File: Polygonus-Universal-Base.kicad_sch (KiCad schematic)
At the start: 11 parts, among them J1 Conn_02x04_Top_Bottom, J4 Polygonus_Plugs, J5 Conn_02x04_Top_Bottom, U1 WBO-Single-Module, U14 WBO-Single-Module

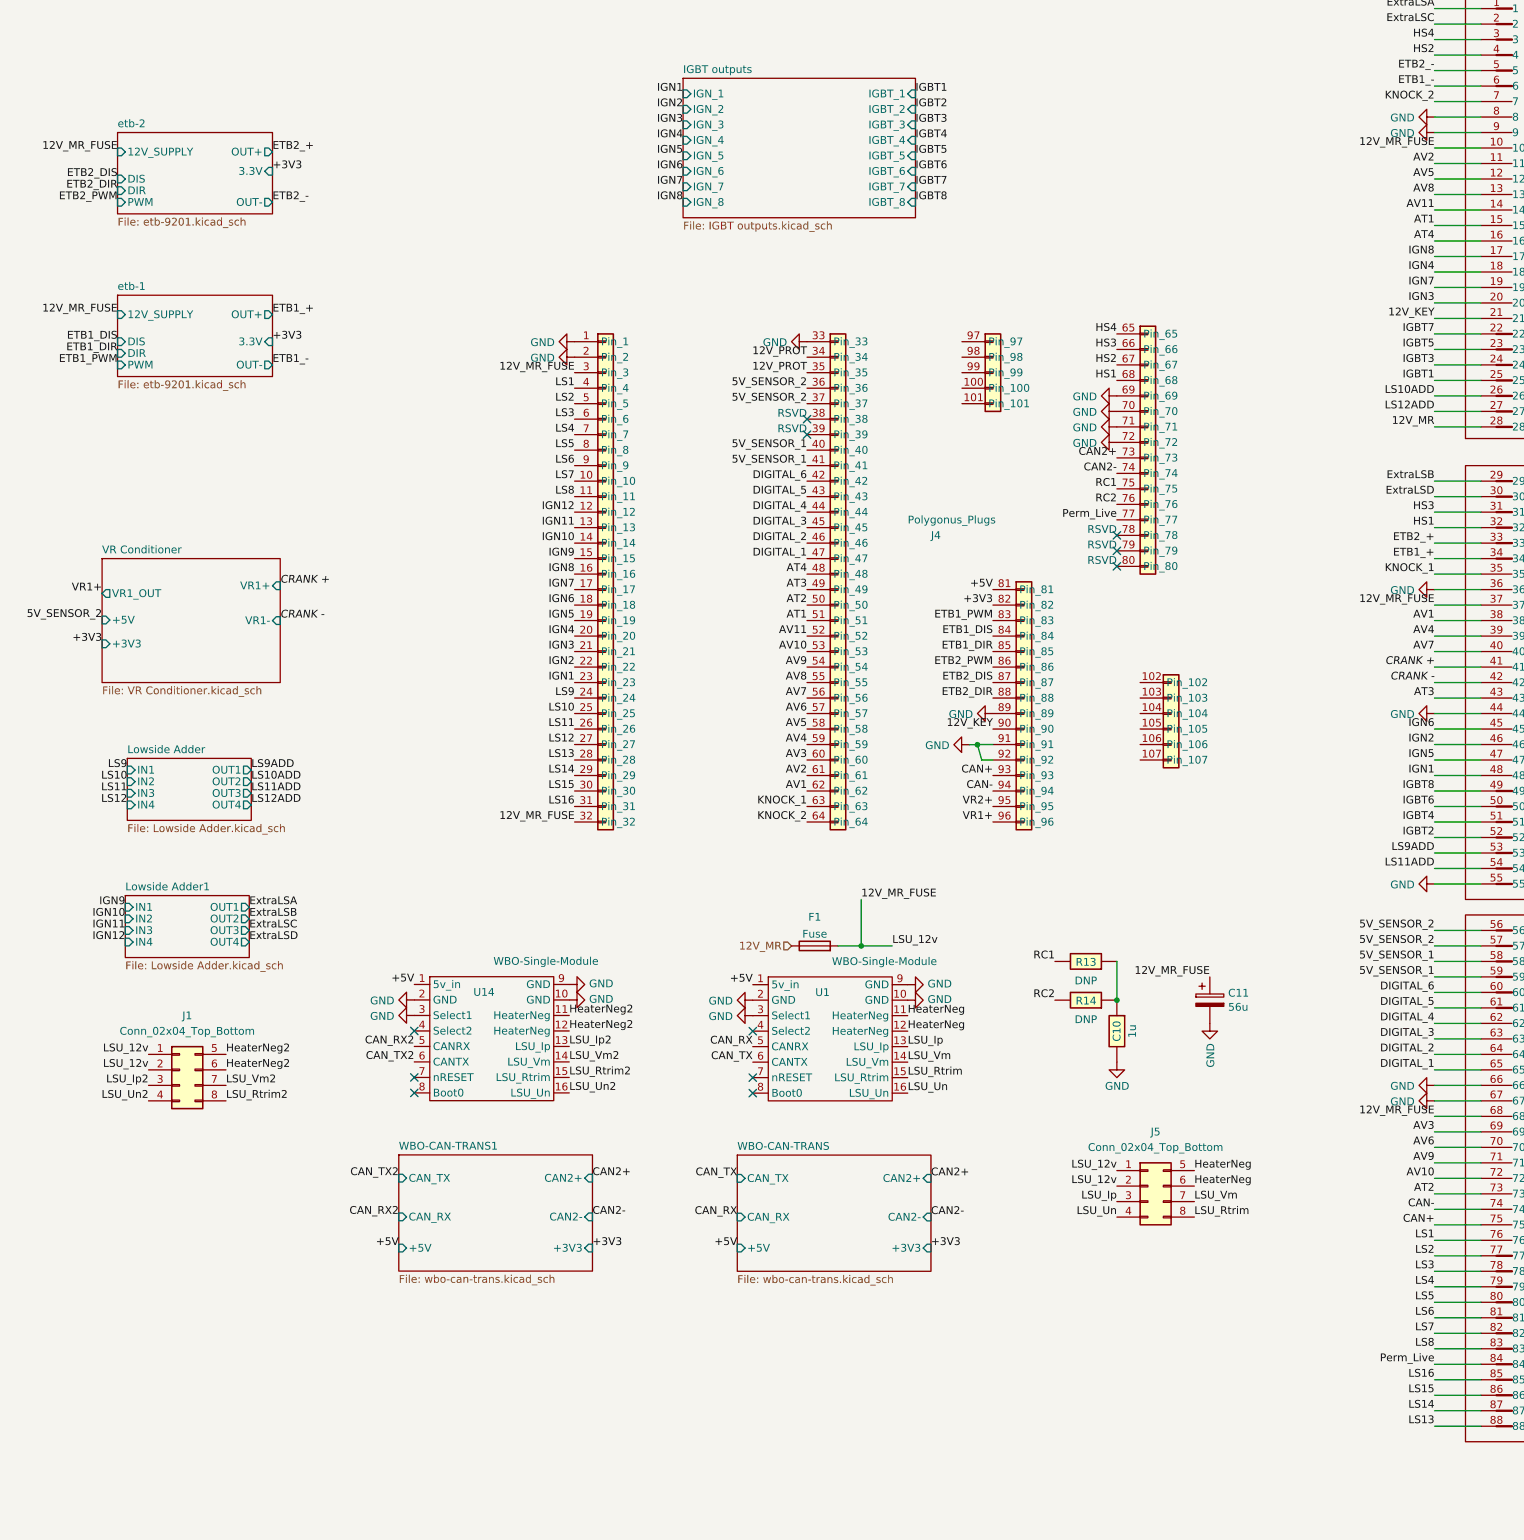
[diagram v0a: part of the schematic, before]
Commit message: fix wideband library, ERC, DRC
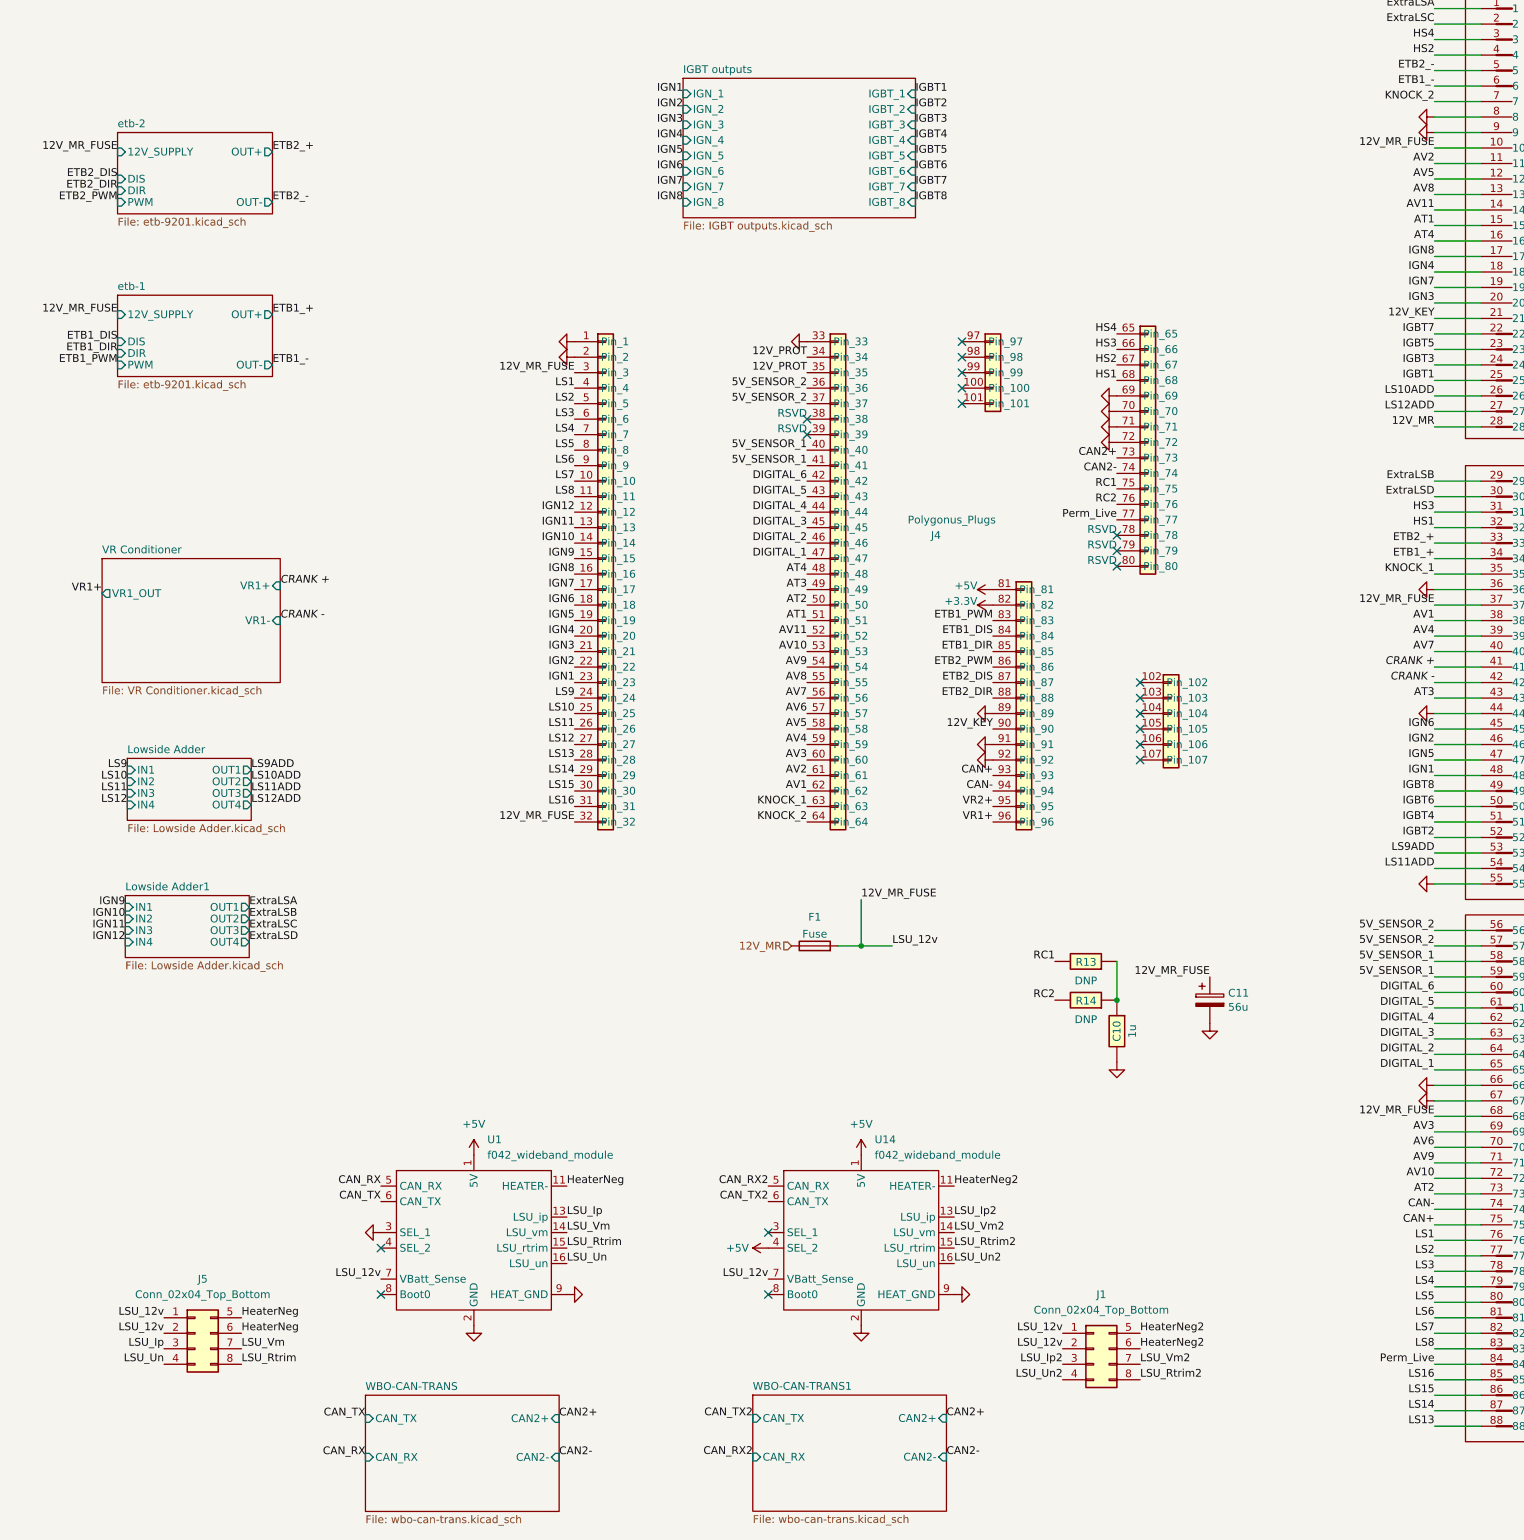
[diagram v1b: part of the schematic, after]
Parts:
- removed U1, U14: WBO-Single-Module, wideband_module:f042_wideband_module, symbol Simon:WBO-Single-Module
- added U1, U14: f042_wideband_module, wideband_module:f042_wideband_module, symbol Wideband:f042_wideband_module
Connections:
- net +5V: now also U1.1 (5V), U14.1 (5V), U14.4 (SEL_2)
- net 12V_MR_FUSE: now also U1.7 (VBatt_Sense), U14.7 (VBatt_Sense)
- net CAN_RX: now also U1.5 (CAN_RX)
- net CAN_RX2: now also U14.5 (CAN_RX)
- net CAN_TX: now also U1.6 (CAN_TX)
- net CAN_TX2: now also U14.6 (CAN_TX)
- net GND: now also U1.10 (HEAT_GND2), U1.2 (GND), U1.3 (SEL_1), U1.9 (HEAT_GND), U14.10 (HEAT_GND2), U14.2 (GND), U14.9 (HEAT_GND)
- net HeaterNeg: now also U1.11 (HEATER-), U1.12 (HEATER-)
- net HeaterNeg2: now also U14.11 (HEATER-), U14.12 (HEATER-)
- net LSU_Ip: now also U1.13 (LSU_ip)
- net LSU_Ip2: now also U14.13 (LSU_ip)
- net LSU_Rtrim: now also U1.15 (LSU_rtrim)
- net LSU_Rtrim2: now also U14.15 (LSU_rtrim)
- net LSU_Un: now also U1.16 (LSU_un)
- net LSU_Un2: now also U14.16 (LSU_un)
- net LSU_Vm: now also U1.14 (LSU_vm)
- net LSU_Vm2: now also U14.14 (LSU_vm)
- net +3V3 renamed +3.3V
- no-connect marks 11 -> 20
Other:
- sheet VR Conditioner ports: added none; removed +3V3, +5V
- sheet WBO-CAN-TRANS ports: added none; removed +3V3, +5V
- sheet WBO-CAN-TRANS1 ports: added none; removed +3V3, +5V
- sheet etb-1 ports: added none; removed 3.3V
- sheet etb-2 ports: added none; removed 3.3V
- moved on the sheet: J1, J5
